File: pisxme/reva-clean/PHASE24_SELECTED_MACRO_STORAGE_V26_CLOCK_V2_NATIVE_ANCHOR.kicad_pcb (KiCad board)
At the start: 6 copper layers, 300 x 180 mm, 14 parts, among them J3 JAE SM3ZS067U410ABR1000 B-key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, J7 Raspberry-Pi-5-Compute-Module, U7 TUSB9261IPVP

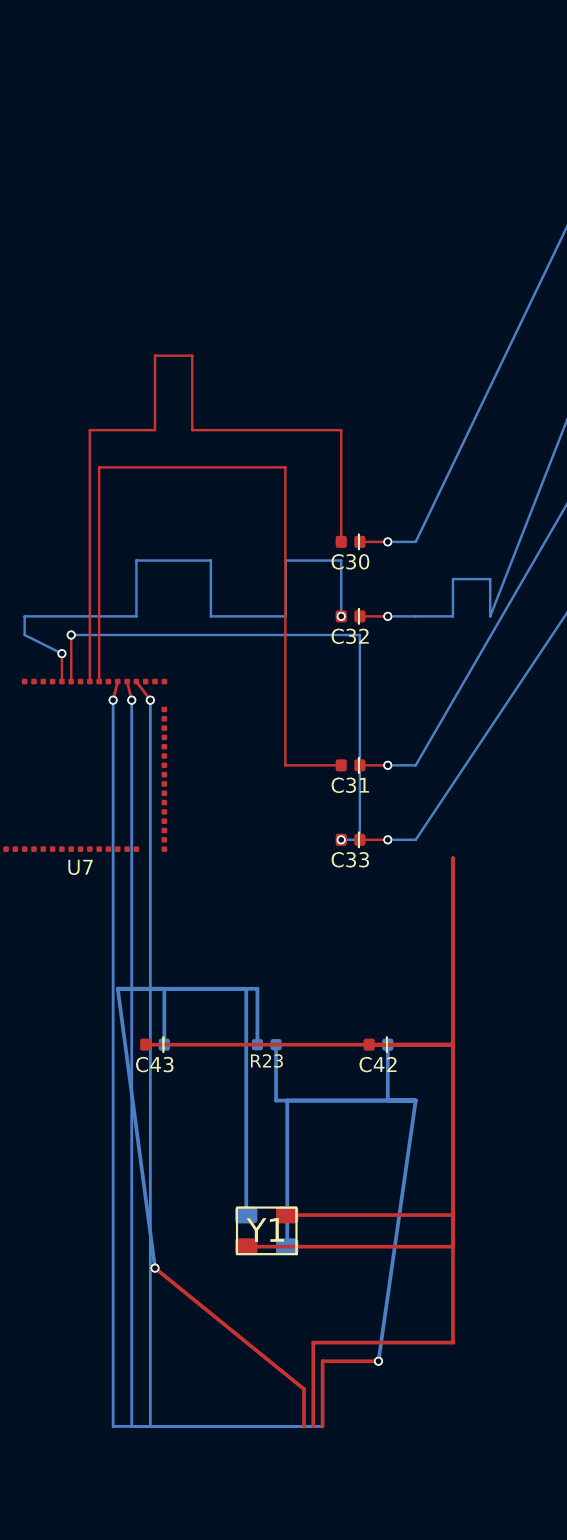
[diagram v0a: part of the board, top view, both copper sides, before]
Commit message: phase24: preserve native clock pad-layer audit
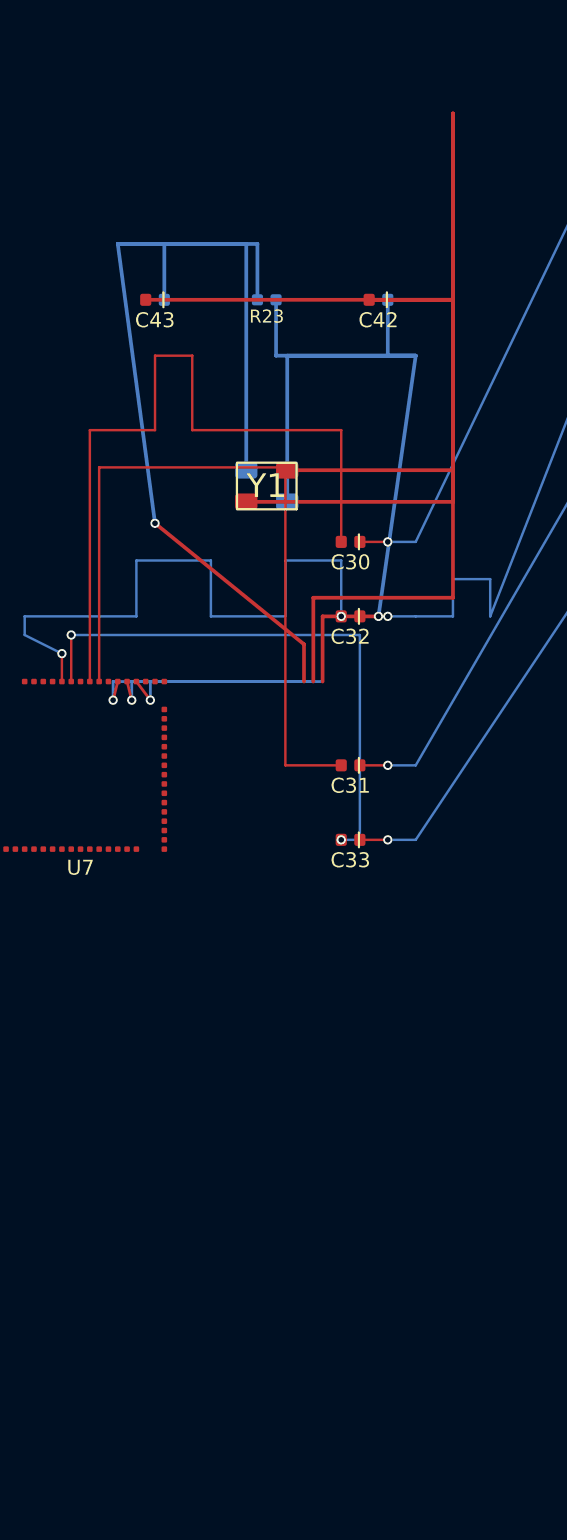
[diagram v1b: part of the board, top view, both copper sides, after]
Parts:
- moved C42 40.0 mm to (112.0, 99.0)
- moved C43 40.0 mm to (100.0, 99.0)
- moved R23 40.0 mm to (106.0, 99.0)
- moved Y1 40.0 mm to (106.0, 109.0)
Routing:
- net /STORAGE/BRIDGE_XO: track 112.8 -> 74.8 mm
- net /STORAGE/BRIDGE_XI: track 99.9 -> 61.9 mm
- net /STORAGE/BRIDGE_VSSOSC: track 188.8 -> 150.8 mm
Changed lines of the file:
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@@
 	(footprint "C_0402_1005Metric"
 		(layer "F.Cu")
-		(at 112 139 180)
+		(at 112 99 180)
 		(property "Reference" "C42"
 			(at 0 -1.1 180)
@@
 	(footprint "C_0402_1005Metric"
 		(layer "F.Cu")
-		(at 100 139 180)
+		(at 100 99 180)
 		(property "Reference" "C43"
 			(at 0 -1.1 180)
@@
 	(footprint "Crystal_3225_4Pad"
 		(layer "F.Cu")
-		(at 106 149 180)
+		(at 106 109 180)
 		(descr "3.2 x 2.5 mm 4-pad crystal; verify vendor pad numbering before release")
 		(property "Reference" "Y1"
@@
 	(footprint "R_0402_1005Metric"
 		(layer "F.Cu")
-		(at 106 139 180)
+		(at 106 99 180)
 		(descr "IPC-7351 nominal 0402 resistor; 1.00 x 0.50 mm body; clean-project commodity passive")
 		(property "Reference" "R23"
@@
 	)
 	(segment
-		(start 109 159.5)
-		(end 109 156)
-		(width 0.2)
+		(start 99 119.5)
+		(end 99.75 120.5)
+		(width 0.15)
 		(layer "F.Cu")
 		(net "/STORAGE/BRIDGE_XI")
 	)
 	(segment
-		(start 109 156)
-		(end 112 156)
+		(start 109 119.5)
+		(end 109 116)
 		(width 0.2)
 		(layer "F.Cu")
@@
 	)
 	(segment
-		(start 99 119.5)
-		(end 99.75 120.5)
-		(width 0.15)
+		(start 109 116)
+		(end 112 116)
+		(width 0.2)
 		(layer "F.Cu")
 		(net "/STORAGE/BRIDGE_XI")
@@
 	)
 	(via
-		(at 112 156)
+		(at 112 116)
 		(size 0.5)
 		(drill 0.3)
@@
 	)
 	(segment
-		(start 114 142)
-		(end 106.5 142)
+		(start 114 102)
+		(end 112.5 102)
 		(width 0.2)
 		(layer "B.Cu")
@@
 	)
 	(segment
-		(start 107.1 142)
-		(end 107.1 149.85)
+		(start 112 116)
+		(end 114 102)
 		(width 0.2)
 		(layer "B.Cu")
@@
 	)
 	(segment
-		(start 112.5 142)
-		(end 112.5 139)
-		(width 0.2)
+		(start 99.75 119.5)
+		(end 109 119.5)
+		(width 0.15)
 		(layer "B.Cu")
 		(net "/STORAGE/BRIDGE_XI")
 	)
 	(segment
-		(start 114 142)
-		(end 107.1 142)
+		(start 107.1 102)
+		(end 107.1 109.85)
 		(width 0.2)
 		(layer "B.Cu")
@@
 	)
 	(segment
-		(start 114 142)
-		(end 112.5 142)
+		(start 106.5 102)
+		(end 106.5 99)
 		(width 0.2)
 		(layer "B.Cu")
@@
 	)
 	(segment
-		(start 99.75 159.5)
-		(end 109 159.5)
+		(start 99.75 120.5)
+		(end 99.75 119.5)
 		(width 0.15)
 		(layer "B.Cu")
@@
 	)
 	(segment
-		(start 99.75 120.5)
-		(end 99.75 159.5)
-		(width 0.15)
+		(start 114 102)
+		(end 106.5 102)
+		(width 0.2)
 		(layer "B.Cu")
 		(net "/STORAGE/BRIDGE_XI")
 	)
 	(segment
-		(start 112 156)
-		(end 114 142)
+		(start 114 102)
+		(end 107.1 102)
 		(width 0.2)
 		(layer "B.Cu")
@@
 	)
 	(segment
-		(start 106.5 142)
-		(end 106.5 139)
+		(start 112.5 102)
+		(end 112.5 99)
 		(width 0.2)
 		(layer "B.Cu")
@@
 	)
 	(segment
-		(start 116 139)
-		(end 99.5 139)
+		(start 116 108.15)
+		(end 107.1 108.15)
 		(width 0.2)
 		(layer "F.Cu")
@@
 	)
 	(segment
-		(start 116 148.15)
-		(end 107.1 148.15)
+		(start 116 99)
+		(end 111.5 99)
 		(width 0.2)
 		(layer "F.Cu")
@@
 	)
 	(segment
-		(start 116 129)
-		(end 116 149.85)
+		(start 116 109.85)
+		(end 104.9 109.85)
 		(width 0.2)
 		(layer "F.Cu")
@@
 	)
 	(segment
-		(start 108.5 159.5)
-		(end 108.5 155)
+		(start 116 89)
+		(end 116 99)
 		(width 0.2)
 		(layer "F.Cu")
@@
 	)
 	(segment
-		(start 116 129)
-		(end 116 148.15)
+		(start 108.5 119.5)
+		(end 108.5 115)
 		(width 0.2)
 		(layer "F.Cu")
@@
 	)
 	(segment
-		(start 98.5 119.5)
-		(end 98.75 120.5)
-		(width 0.15)
+		(start 116 115)
+		(end 116 89)
+		(width 0.2)
 		(layer "F.Cu")
 		(net "/STORAGE/BRIDGE_VSSOSC")
 	)
 	(segment
-		(start 116 149.85)
-		(end 104.9 149.85)
+		(start 116 99)
+		(end 99.5 99)
 		(width 0.2)
 		(layer "F.Cu")
@@
 	)
 	(segment
-		(start 108.5 155)
-		(end 116 155)
+		(start 108.5 115)
+		(end 116 115)
 		(width 0.2)
 		(layer "F.Cu")
@@
 	)
 	(segment
-		(start 116 139)
-		(end 111.5 139)
+		(start 116 89)
+		(end 116 99)
 		(width 0.2)
 		(layer "F.Cu")
@@
 	)
 	(segment
-		(start 116 129)
-		(end 116 139)
+		(start 116 89)
+		(end 116 109.85)
 		(width 0.2)
 		(layer "F.Cu")
@@
 	)
 	(segment
-		(start 116 155)
-		(end 116 129)
-		(width 0.2)
+		(start 98.5 119.5)
+		(end 98.75 120.5)
+		(width 0.15)
 		(layer "F.Cu")
 		(net "/STORAGE/BRIDGE_VSSOSC")
 	)
 	(segment
-		(start 116 129)
-		(end 116 139)
+		(start 116 89)
+		(end 116 108.15)
 		(width 0.2)
 		(layer "F.Cu")
@@
 	(segment
 		(start 98.75 120.5)
-		(end 98.75 159.5)
+		(end 98.75 119.5)
 		(width 0.15)
 		(layer "B.Cu")
@@
 	)
 	(segment
-		(start 98.75 159.5)
-		(end 108.5 159.5)
+		(start 98.75 119.5)
+		(end 108.5 119.5)
 		(width 0.15)
 		(layer "B.Cu")
@@
 	)
 	(segment
-		(start 108 159.5)
-		(end 108 157.5)
+		(start 108 117.5)
+		(end 100 111)
 		(width 0.2)
 		(layer "F.Cu")
@@
 	)
 	(segment
-		(start 108 157.5)
-		(end 100 151)
+		(start 108 119.5)
+		(end 108 117.5)
 		(width 0.2)
 		(layer "F.Cu")
@@
 	)
 	(via
-		(at 100 151)
+		(at 97.75 120.5)
 		(size 0.5)
 		(drill 0.3)
@@
 	)
 	(via
-		(at 97.75 120.5)
+		(at 100 111)
 		(size 0.5)
 		(drill 0.3)
@@
 	)
 	(segment
-		(start 100.5 136)
-		(end 100.5 139)
+		(start 98 96)
+		(end 100.5 96)
 		(width 0.2)
 		(layer "B.Cu")
@@
 	)
 	(segment
-		(start 97.75 159.5)
-		(end 108 159.5)
-		(width 0.15)
+		(start 100.5 96)
+		(end 100.5 99)
+		(width 0.2)
 		(layer "B.Cu")
 		(net "/STORAGE/BRIDGE_XO")
 	)
 	(segment
-		(start 104.9 136)
-		(end 104.9 148.15)
-		(width 0.2)
+		(start 97.75 119.5)
+		(end 108 119.5)
+		(width 0.15)
 		(layer "B.Cu")
 		(net "/STORAGE/BRIDGE_XO")
 	)
 	(segment
-		(start 98 136)
-		(end 104.9 136)
-		(width 0.2)
+		(start 97.75 120.5)
+		(end 97.75 119.5)
+		(width 0.15)
 		(layer "B.Cu")
 		(net "/STORAGE/BRIDGE_XO")
 	)
 	(segment
-		(start 98 136)
-		(end 105.5 136)
+		(start 98 96)
+		(end 104.9 96)
 		(width 0.2)
 		(layer "B.Cu")
@@
 	)
 	(segment
-		(start 98 136)
-		(end 100.5 136)
+		(start 98 96)
+		(end 105.5 96)
 		(width 0.2)
 		(layer "B.Cu")
@@
 	)
 	(segment
-		(start 97.75 120.5)
-		(end 97.75 159.5)
-		(width 0.15)
+		(start 105.5 96)
+		(end 105.5 99)
+		(width 0.2)
 		(layer "B.Cu")
 		(net "/STORAGE/BRIDGE_XO")
 	)
 	(segment
-		(start 100 151)
-		(end 98 136)
+		(start 100 111)
+		(end 98 96)
 		(width 0.2)
 		(layer "B.Cu")
@@
 	)
 	(segment
-		(start 105.5 136)
-		(end 105.5 139)
+		(start 104.9 96)
+		(end 104.9 108.15)
 		(width 0.2)
 		(layer "B.Cu")
